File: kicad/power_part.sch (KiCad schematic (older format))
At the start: 24 parts, among them Q10 BSC016N06NS, Q11 BSC016N06NS, Q12 BSC016N06NS, Q13 BSC016N06NS, Q14 BSS138

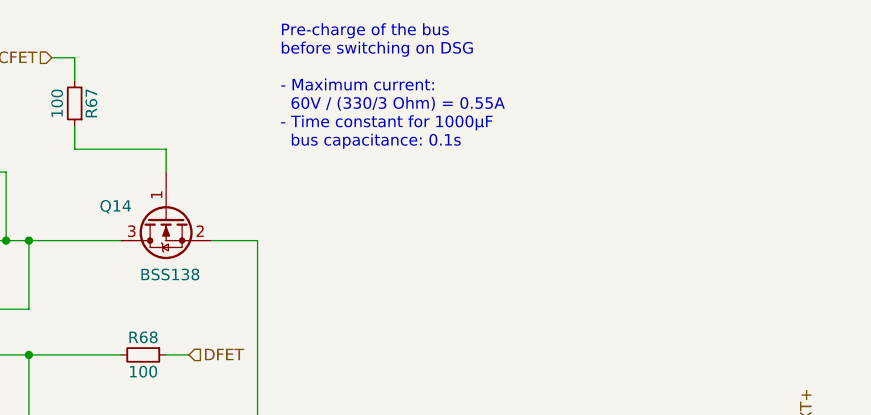
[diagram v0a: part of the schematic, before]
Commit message: Fix issues found during testing (v0.1.1)
- Add BAT+/- and EXT+/- markings to terminals (#2)
- Change C30 to 470nF (#5)
- Add C20 (47nF) at VC0 pin (#5)
- Add C21 and R72 for proper low-pass filter of VDD (#5)
- Change C39 at VREF to 1uF (#5)
- Add R70: Pull-down for PCHG FET (#5)
- Add R73: Weak pull-down for 5V supply (#6)
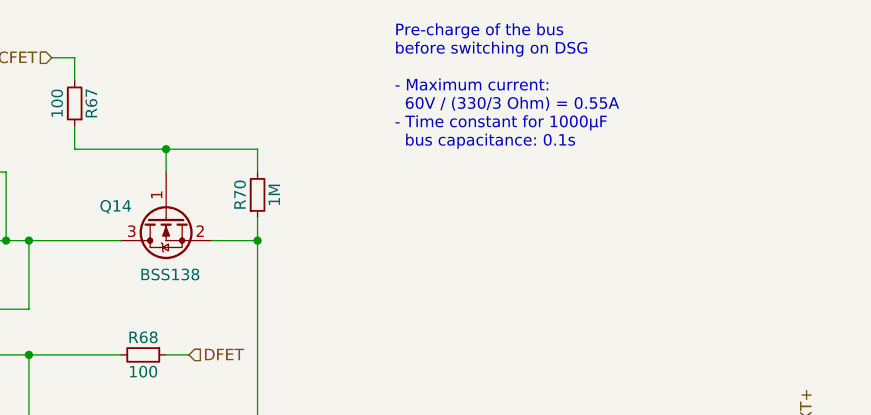
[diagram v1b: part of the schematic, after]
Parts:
- added R70: 1M, LibreSolar:R_0603_1608, symbol Project:R
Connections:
- net EXT+: now also R70.1
- net at Q14.1 (G), R67.1: now also R70.2
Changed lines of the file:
@@
 EESchema Schematic File Version 4
-LIBS:bms-8s50-ic-cache
-EELAYER 29 0
+EELAYER 30 0
 EELAYER END
 $Descr A4 11693 8268
@@
 Sheet 3 5
 Title "BMS 8S50 IC"
-Date "2019-03-04"
-Rev "0.1"
+Date "2020-05-08"
+Rev "0.1.1"
 Comp "Libre Solar"
 Comment1 "Author: Martin Jäger"
@@
 	0    1    1    0
 $EndComp
-Text Notes 7100 1900 0    50   ~ 0
+Text Notes 7600 1900 0    50   ~ 0
 Pre-charge of the bus\nbefore switching on DSG\n\n- Maximum current:\n  60V / (330/3 Ohm) = 0.55A\n- Time constant for 1000µF\n  bus capacitance: 0.1s
 Text Notes 2300 3700 0    50   ~ 0
@@
 	7900 4200 7900 5000
 Connection ~ 7400 5000
+$Comp
+L Project:R R70
+U 1 1 5EF7F82F
+P 7000 2100
+F 0 "R70" V 6925 2100 50  0000 C CNN
+F 1 "1M" V 7075 2100 50  0000 C CNN
+F 2 "LibreSolar:R_0603_1608" V 6825 2000 50  0001 C CNN
+F 3 "" H 7000 2100 50  0000 C CNN
+F 4 "Yageo" H 2200 -500 60  0001 C CNN "Manufacturer"
+F 5 "RC0603FR-071ML" H 2200 -500 60  0001 C CNN "PartNumber"
+	1    7000 2100
+	1    0    0    1
+$EndComp
+Wire Wire Line
+	7000 2000 7000 1900
+Wire Wire Line
+	7000 1900 6600 1900
+Connection ~ 6600 1900
+Wire Wire Line
+	7000 2200 7000 2300
+Connection ~ 7000 2300
 $EndSCHEMATC

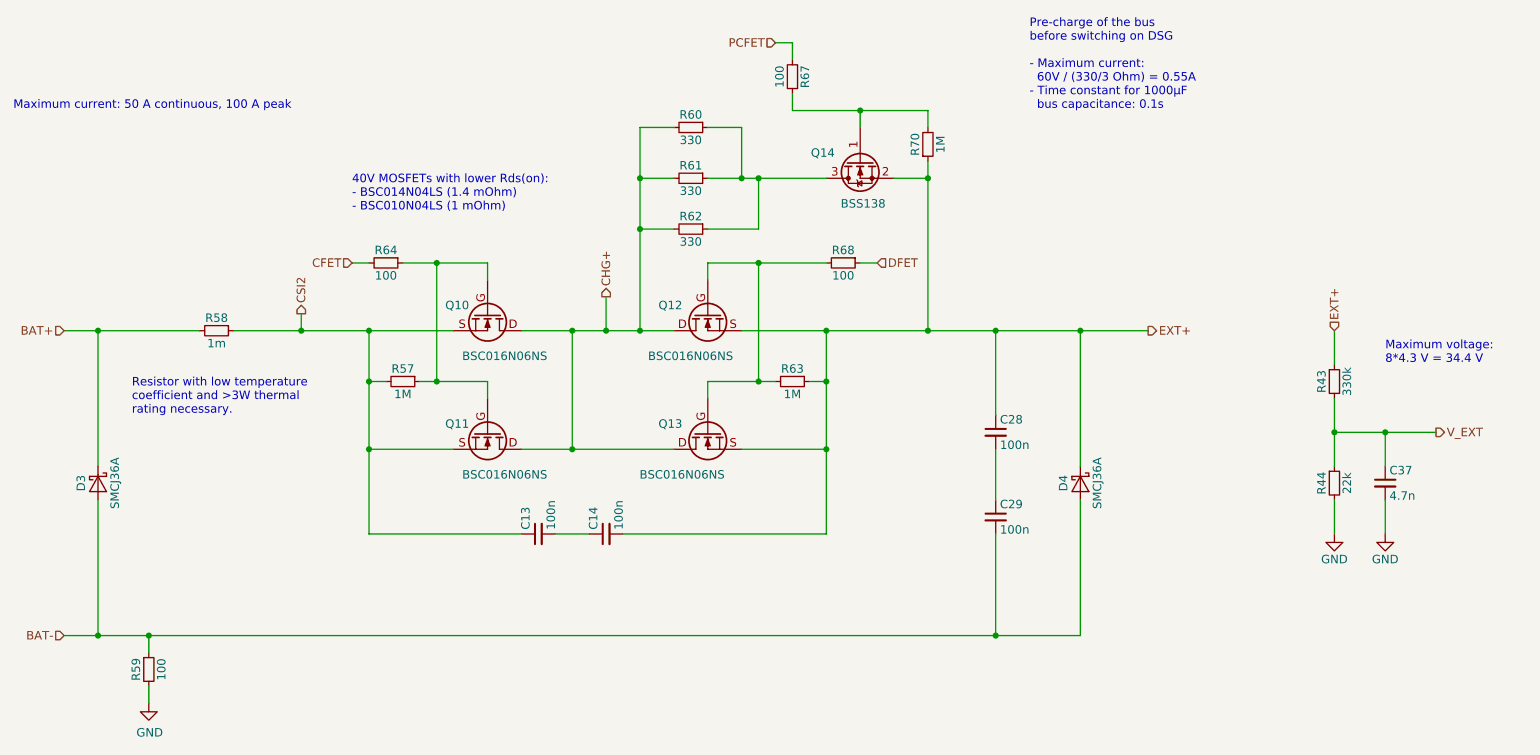
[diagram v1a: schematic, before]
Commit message: Update to v0.2
- Switch to STM32L452 MCU (STM32F072 has too little RAM for CAN ISO-TP etc.)
- Add CAN termination jumper
- Add CAN bus power supply diodes
- Update CAN connector to match LS.bus spec
- Add interactive BOM and CSV BOM to build directory
- Add additional thermal vias with 0.2mm diameter under MOSFETs
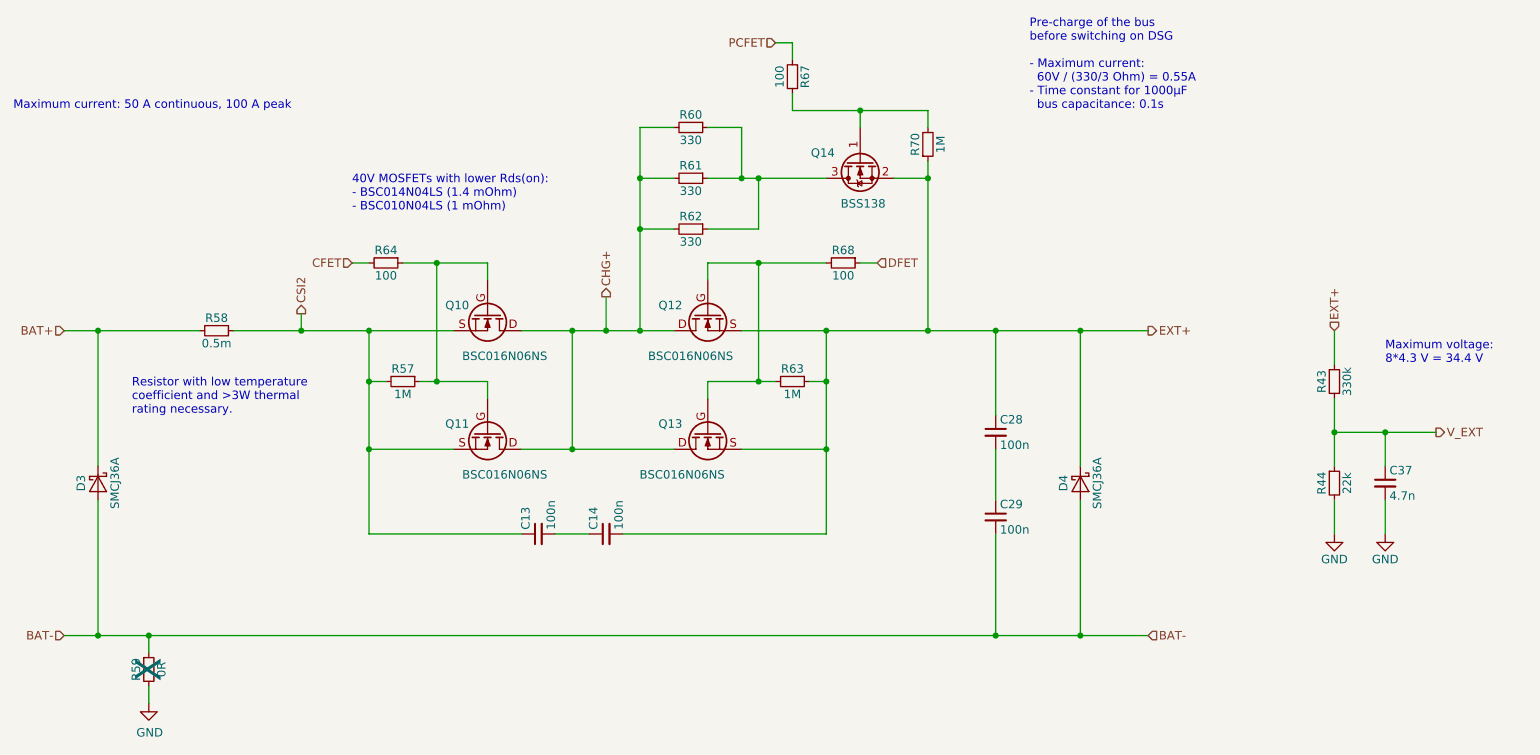
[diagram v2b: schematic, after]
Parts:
- R58: value 1m -> 0.5m; PartNumber WSLF25121L000FEA -> WSLF2512L5000FEA; Remarks Alternative: Bourns CSS2H-2512R-1L00F -> Alternative: Bourns CSS2H-2512R-L500F
- R59: value 100 -> 0R; Config (none) -> +test; DNF (none) -> X; PartNumber RC0603FR-07100RL -> RC0603FR-070RL; Remarks (none) -> Only for testing
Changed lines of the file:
@@
 Sheet 3 5
 Title "BMS 8S50 IC"
-Date "2020-05-08"
-Rev "0.1.1"
-Comp "Libre Solar"
-Comment1 "Author: Martin Jäger"
-Comment2 ""
-Comment3 ""
+Date "2021-02-13"
+Rev "0.2"
+Comp "Libre Solar Technologies GmbH"
+Comment1 "Website: https://libre.solar"
+Comment2 "Author: Martin Jäger"
+Comment3 "License: Creative Commons Attribution-ShareAlike 4.0 International"
 Comment4 ""
 $EndDescr
@@
 P 2800 3200
 F 0 "R58" V 2725 3200 50  0000 C CNN
-F 1 "1m" V 2875 3200 50  0000 C CNN
+F 1 "0.5m" V 2875 3200 50  0000 C CNN
 F 2 "LibreSolar:R_Shunt_2512" V 2625 3100 50  0001 C CNN
 F 3 "" H 2800 3200 50  0000 C CNN
 F 4 "Vishay / Dale" H 2800 3200 60  0001 C CNN "Manufacturer"
-F 5 "WSLF25121L000FEA" H 2800 3200 60  0001 C CNN "PartNumber"
-F 6 "Alternative: Bourns CSS2H-2512R-1L00F" H 2800 3200 50  0001 C CNN "Remarks"
+F 5 "WSLF2512L5000FEA" H 2800 3200 60  0001 C CNN "PartNumber"
+F 6 "Alternative: Bourns CSS2H-2512R-L500F" H 2800 3200 50  0001 C CNN "Remarks"
 	1    2800 3200
 	0    1    1    0
@@
 AR Path="/5CC2B452/5CC5BC5F" Ref="R59"  Part="1"
 F 0 "R59" V 2325 5200 50  0000 C CNN
-F 1 "100" V 2475 5200 50  0000 C CNN
+F 1 "0R" V 2475 5200 50  0000 C CNN
 F 2 "LibreSolar:R_0603_1608" V 2225 5100 50  0001 C CNN
 F 3 "" H 2400 5200 50  0000 C CNN
 F 4 "Yageo" H -1500 2050 50  0001 C CNN "Manufacturer"
-F 5 "RC0603FR-07100RL" H -1500 2050 50  0001 C CNN "PartNumber"
+F 5 "RC0603FR-070RL" H -1500 2050 50  0001 C CNN "PartNumber"
+F 6 "X" V 2400 5200 150 0000 C CNN "DNF"
+F 7 "+test" H 2400 5200 50  0001 C CNN "Config"
+F 8 "Only for testing" H 2400 5200 50  0001 C CNN "Remarks"
 	1    2400 5200
 	1    0    0    -1
@@
 	7000 2200 7000 2300
 Connection ~ 7000 2300
+Text HLabel 8300 5000 2    50   Input ~ 0
+BAT-
+Wire Wire Line
+	8300 5000 7900 5000
+Connection ~ 7900 5000
 $EndSCHEMATC
